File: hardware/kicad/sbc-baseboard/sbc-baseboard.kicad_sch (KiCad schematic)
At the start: 4 parts

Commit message: Re-lay out every sheet around its main component
Nets fan out of each hub IC as wires at pin pitch; connectors, series
parts, pull-ups and power symbols sit at the lane ends, and labels are
kept for nets that leave the page. Supply pins share a bus with their
decoupling; ESD arrays sit on the connector's D-/D+ rows and port
switches on the VBUS row, so every wire into a receptacle is straight;
the stacked USB-A is a two-unit symbol, one per port. Relays move to
their own sheet (8xx). ESD diodes use KiCad's PESD5V0S1UL in SOD-882.

Generator: gen/fanout.py (lane engine), gen/check_geom.py (endpoint
contacts), gen/netcheck.py (wire-level rail merges). ERC, both checks
and a renumbering-tolerant netlist diff against the first pass all
clean; 331 parts, 354 nets.

Co-Authored-By: Claude Fable 5.1 <noreply@anthropic.com>
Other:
- added sheet Relays (relays.kicad_sch)
- note added: "- K803 JW1FSN contact pad mapping (COM 6 / NO 4 / NC 2) against the Panasonic drawing"
- note added: "Reference designators: 1xx power, 2xx MCU, 3xx Ethernet, 4xx hub, 5xx FTDI, 6xx DAPLink, 7xx target I/O, 8xx relays and passthrough."
- note removed: "- K703 JW1FSN contact pad mapping (COM 6 / NO 4 / NC 2) against the Panasonic drawing"
- note removed: "Reference designators: 1xx power, 2xx MCU, 3xx Ethernet, 4xx hub, 5xx FTDI, 6xx DAPLink, 7xx target I/O."
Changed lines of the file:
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@@
 		(instances
 			(project "sbc-baseboard"
-				(path "/f7384331-47cf-4f51-a3a4-f7288a6fca1f"
+				(path "/67f2ab7f-7b0b-43bf-9ea7-cdb92436ed71"
 					(page "2")
 				)
@@
 		(instances
 			(project "sbc-baseboard"
-				(path "/f7384331-47cf-4f51-a3a4-f7288a6fca1f"
+				(path "/67f2ab7f-7b0b-43bf-9ea7-cdb92436ed71"
 					(page "3")
 				)
@@
 		(instances
 			(project "sbc-baseboard"
-				(path "/f7384331-47cf-4f51-a3a4-f7288a6fca1f"
+				(path "/67f2ab7f-7b0b-43bf-9ea7-cdb92436ed71"
 					(page "4")
 				)
@@
 		(instances
 			(project "sbc-baseboard"
-				(path "/f7384331-47cf-4f51-a3a4-f7288a6fca1f"
+				(path "/67f2ab7f-7b0b-43bf-9ea7-cdb92436ed71"
 					(page "5")
 				)
@@
 		(instances
 			(project "sbc-baseboard"
-				(path "/f7384331-47cf-4f51-a3a4-f7288a6fca1f"
+				(path "/67f2ab7f-7b0b-43bf-9ea7-cdb92436ed71"
 					(page "6")
 				)
@@
 		(instances
 			(project "sbc-baseboard"
-				(path "/f7384331-47cf-4f51-a3a4-f7288a6fca1f"
+				(path "/67f2ab7f-7b0b-43bf-9ea7-cdb92436ed71"
 					(page "7")
 				)
@@
 		(instances
 			(project "sbc-baseboard"
-				(path "/f7384331-47cf-4f51-a3a4-f7288a6fca1f"
+				(path "/67f2ab7f-7b0b-43bf-9ea7-cdb92436ed71"
 					(page "8")
+				)
+			)
+		)
+	)
+	(sheet
+		(at 210 80)
+		(size 50 25)
+		(exclude_from_sim no)
+		(in_bom yes)
+		(on_board yes)
+		(dnp no)
+		(fields_autoplaced yes)
+		(stroke
+			(width 0.1524)
+			(type solid)
+		)
+		(fill
+			(color 0 0 0 0)
+		)
+		(property "Sheetname" "Relays"
+			(at 210 79.2884 0)
+			(show_name no)
+			(do_not_autoplace no)
+			(effects
+				(font
+					(size 1.27 1.27)
+				)
+				(justify left bottom)
+			)
+		)
+		(property "Sheetfile" "relays.kicad_sch"
+			(at 210 105.5846 0)
+			(show_name no)
+			(do_not_autoplace no)
+			(effects
+				(font
+					(size 1.27 1.27)
+				)
+				(justify left top)
+			)
+		)
+		(instances
+			(project "sbc-baseboard"
+				(path "/67f2ab7f-7b0b-43bf-9ea7-cdb92436ed71"
+					(page "9")
 				)
 			)
@@
 		(instances
 			(project "sbc-baseboard"
-				(path "/f7384331-47cf-4f51-a3a4-f7288a6fca1f"
+				(path "/67f2ab7f-7b0b-43bf-9ea7-cdb92436ed71"
 					(reference "H1")
 					(unit 1)
@@
 		(instances
 			(project "sbc-baseboard"
-				(path "/f7384331-47cf-4f51-a3a4-f7288a6fca1f"
+				(path "/67f2ab7f-7b0b-43bf-9ea7-cdb92436ed71"
 					(reference "#PWR01001")
 					(unit 1)
@@
 		(instances
 			(project "sbc-baseboard"
-				(path "/f7384331-47cf-4f51-a3a4-f7288a6fca1f"
+				(path "/67f2ab7f-7b0b-43bf-9ea7-cdb92436ed71"
 					(reference "H2")
 					(unit 1)
@@
 		(instances
 			(project "sbc-baseboard"
-				(path "/f7384331-47cf-4f51-a3a4-f7288a6fca1f"
+				(path "/67f2ab7f-7b0b-43bf-9ea7-cdb92436ed71"
 					(reference "#PWR01002")
 					(unit 1)
@@
 		(instances
 			(project "sbc-baseboard"
-				(path "/f7384331-47cf-4f51-a3a4-f7288a6fca1f"
+				(path "/67f2ab7f-7b0b-43bf-9ea7-cdb92436ed71"
 					(reference "H3")
 					(unit 1)
@@
 		(instances
 			(project "sbc-baseboard"
-				(path "/f7384331-47cf-4f51-a3a4-f7288a6fca1f"
+				(path "/67f2ab7f-7b0b-43bf-9ea7-cdb92436ed71"
 					(reference "#PWR01003")
 					(unit 1)
@@
 		(instances
 			(project "sbc-baseboard"
-				(path "/f7384331-47cf-4f51-a3a4-f7288a6fca1f"
+				(path "/67f2ab7f-7b0b-43bf-9ea7-cdb92436ed71"
 					(reference "H4")
 					(unit 1)
@@
 		(instances
 			(project "sbc-baseboard"
-				(path "/f7384331-47cf-4f51-a3a4-f7288a6fca1f"
+				(path "/67f2ab7f-7b0b-43bf-9ea7-cdb92436ed71"
 					(reference "#PWR01004")
 					(unit 1)
@@
 		)
 	)
-	(text "  - K703 JW1FSN contact pad mapping (COM 6 / NO 4 / NC 2) against the Panasonic drawing"
+	(text "  - K803 JW1FSN contact pad mapping (COM 6 / NO 4 / NC 2) against the Panasonic drawing"
 		(exclude_from_sim no)
 		(at 30 194.2 0)
@@
 		)
 	)
-	(text "Reference designators: 1xx power, 2xx MCU, 3xx Ethernet, 4xx hub, 5xx FTDI, 6xx DAPLink, 7xx target I/O."
+	(text "Reference designators: 1xx power, 2xx MCU, 3xx Ethernet, 4xx hub, 5xx FTDI, 6xx DAPLink, 7xx target I/O, 8xx relays and passthrough."
 		(exclude_from_sim no)
 		(at 30 213.4 0)

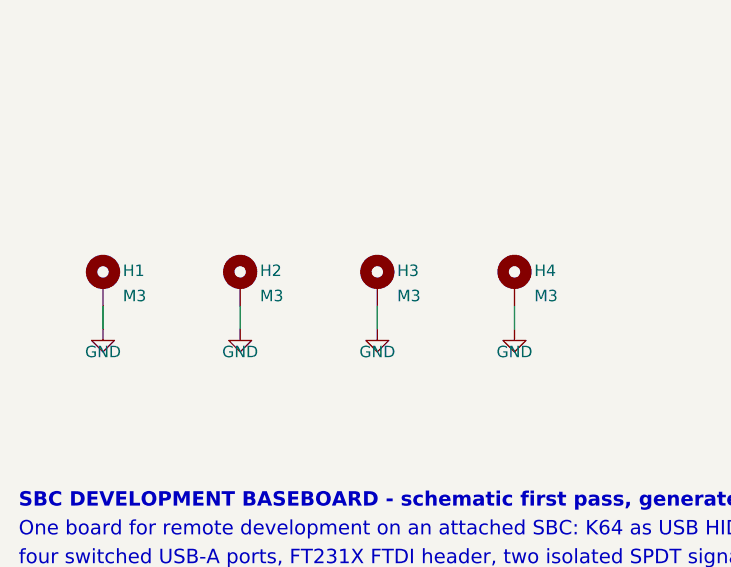
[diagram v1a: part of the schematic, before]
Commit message: Symbol direction, field text and decoupling ladders across every sheet
Every GND symbol now hangs down and every rail stands up: decoupling
hangs from the supply bus into a GND rail with one GND symbol at the end
(ladders), rails on crowded supply pins are jogged sideways, the SWD
header is mirrored instead of rotated. Field text on in-line parts reads
horizontally (KiCad adds the symbol rotation to the field angle) and is
placed by lane direction; hanging parts carry their text on the side away
from the pin; IC reference and value sit where the library put them.
Power sheet: bus buffer moved under the STUSB4500's I2C lanes with direct
routes, programmer by label, buck drawn as a box with its input and
output capacitors as ladders. New gen/check_layout.py reports text and
wire overlaps and wrong-way power symbols; PDF export draws hop-overs.

ERC 0, no merged rails, netlist equivalent; text-overlap residue listed
in the layout checker output remains on the hub, relays and DAPLink.

Co-Authored-By: Claude Fable 5.1 <noreply@anthropic.com>
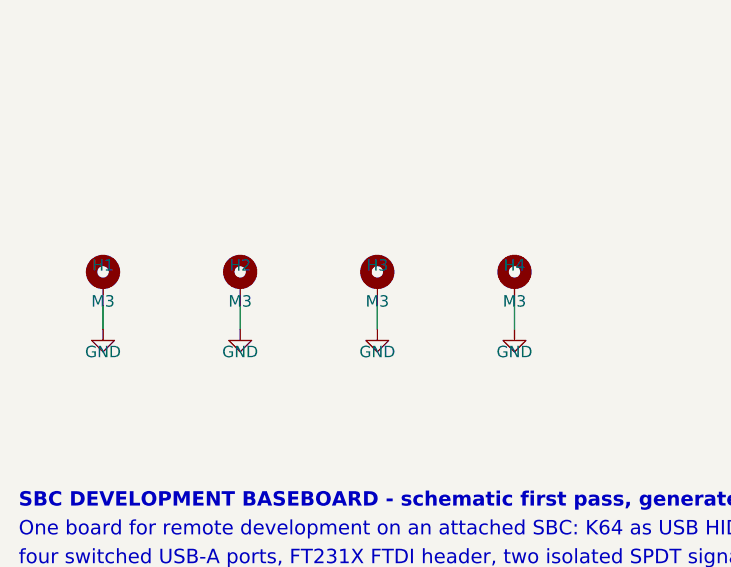
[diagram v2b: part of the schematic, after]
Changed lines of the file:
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@@
 		(instances
 			(project "sbc-baseboard"
-				(path "/67f2ab7f-7b0b-43bf-9ea7-cdb92436ed71"
+				(path "/720ca2c9-6349-4d12-b50d-43ef6cb86535"
 					(page "2")
 				)
@@
 		(instances
 			(project "sbc-baseboard"
-				(path "/67f2ab7f-7b0b-43bf-9ea7-cdb92436ed71"
+				(path "/720ca2c9-6349-4d12-b50d-43ef6cb86535"
 					(page "3")
 				)
@@
 		(instances
 			(project "sbc-baseboard"
-				(path "/67f2ab7f-7b0b-43bf-9ea7-cdb92436ed71"
+				(path "/720ca2c9-6349-4d12-b50d-43ef6cb86535"
 					(page "4")
 				)
@@
 		(instances
 			(project "sbc-baseboard"
-				(path "/67f2ab7f-7b0b-43bf-9ea7-cdb92436ed71"
+				(path "/720ca2c9-6349-4d12-b50d-43ef6cb86535"
 					(page "5")
 				)
@@
 		(instances
 			(project "sbc-baseboard"
-				(path "/67f2ab7f-7b0b-43bf-9ea7-cdb92436ed71"
+				(path "/720ca2c9-6349-4d12-b50d-43ef6cb86535"
 					(page "6")
 				)
@@
 		(instances
 			(project "sbc-baseboard"
-				(path "/67f2ab7f-7b0b-43bf-9ea7-cdb92436ed71"
+				(path "/720ca2c9-6349-4d12-b50d-43ef6cb86535"
 					(page "7")
 				)
@@
 		(instances
 			(project "sbc-baseboard"
-				(path "/67f2ab7f-7b0b-43bf-9ea7-cdb92436ed71"
+				(path "/720ca2c9-6349-4d12-b50d-43ef6cb86535"
 					(page "8")
 				)
@@
 		(instances
 			(project "sbc-baseboard"
-				(path "/67f2ab7f-7b0b-43bf-9ea7-cdb92436ed71"
+				(path "/720ca2c9-6349-4d12-b50d-43ef6cb86535"
 					(page "9")
 				)
@@
 		(fields_autoplaced no)
 		(property "Reference" "H1"
-			(at 41.57 148.46 0)
-			(show_name no)
-			(do_not_autoplace no)
-			(effects
-				(font
-					(size 1.27 1.27)
-				)
-				(justify left)
+			(at 39.37 147.86 0)
+			(show_name no)
+			(do_not_autoplace no)
+			(effects
+				(font
+					(size 1.27 1.27)
+				)
 			)
 		)
 		(property "Value" "M3"
-			(at 41.57 151.26 0)
-			(show_name no)
-			(do_not_autoplace no)
-			(effects
-				(font
-					(size 1.27 1.27)
-				)
-				(justify left)
+			(at 39.37 151.86 0)
+			(show_name no)
+			(do_not_autoplace no)
+			(effects
+				(font
+					(size 1.27 1.27)
+				)
 			)
 		)
@@
 					(size 1.27 1.27)
 				)
-				(justify left)
 			)
 		)
@@
 					(size 1.27 1.27)
 				)
-				(justify left)
 			)
 		)
@@
 					(size 1.27 1.27)
 				)
-				(justify left)
 			)
 		)
@@
 		(instances
 			(project "sbc-baseboard"
-				(path "/67f2ab7f-7b0b-43bf-9ea7-cdb92436ed71"
+				(path "/720ca2c9-6349-4d12-b50d-43ef6cb86535"
 					(reference "H1")
 					(unit 1)
@@
 		(instances
 			(project "sbc-baseboard"
-				(path "/67f2ab7f-7b0b-43bf-9ea7-cdb92436ed71"
+				(path "/720ca2c9-6349-4d12-b50d-43ef6cb86535"
 					(reference "#PWR01001")
 					(unit 1)
@@
 		(fields_autoplaced no)
 		(property "Reference" "H2"
-			(at 56.81 148.46 0)
-			(show_name no)
-			(do_not_autoplace no)
-			(effects
-				(font
-					(size 1.27 1.27)
-				)
-				(justify left)
+			(at 54.61 147.86 0)
+			(show_name no)
+			(do_not_autoplace no)
+			(effects
+				(font
+					(size 1.27 1.27)
+				)
 			)
 		)
 		(property "Value" "M3"
-			(at 56.81 151.26 0)
-			(show_name no)
-			(do_not_autoplace no)
-			(effects
-				(font
-					(size 1.27 1.27)
-				)
-				(justify left)
+			(at 54.61 151.86 0)
+			(show_name no)
+			(do_not_autoplace no)
+			(effects
+				(font
+					(size 1.27 1.27)
+				)
 			)
 		)
@@
 					(size 1.27 1.27)
 				)
-				(justify left)
 			)
 		)
@@
 					(size 1.27 1.27)
 				)
-				(justify left)
 			)
 		)
@@
 					(size 1.27 1.27)
 				)
-				(justify left)
 			)
 		)
@@
 		(instances
 			(project "sbc-baseboard"
-				(path "/67f2ab7f-7b0b-43bf-9ea7-cdb92436ed71"
+				(path "/720ca2c9-6349-4d12-b50d-43ef6cb86535"
 					(reference "H2")
 					(unit 1)
@@
 		(instances
 			(project "sbc-baseboard"
-				(path "/67f2ab7f-7b0b-43bf-9ea7-cdb92436ed71"
+				(path "/720ca2c9-6349-4d12-b50d-43ef6cb86535"
 					(reference "#PWR01002")
 					(unit 1)
@@
 		(fields_autoplaced no)
 		(property "Reference" "H3"
-			(at 72.05 148.46 0)
-			(show_name no)
-			(do_not_autoplace no)
-			(effects
-				(font
-					(size 1.27 1.27)
-				)
-				(justify left)
+			(at 69.85 147.86 0)
+			(show_name no)
+			(do_not_autoplace no)
+			(effects
+				(font
+					(size 1.27 1.27)
+				)
 			)
 		)
 		(property "Value" "M3"
-			(at 72.05 151.26 0)
-			(show_name no)
-			(do_not_autoplace no)
-			(effects
-				(font
-					(size 1.27 1.27)
-				)
-				(justify left)
+			(at 69.85 151.86 0)
+			(show_name no)
+			(do_not_autoplace no)
+			(effects
+				(font
+					(size 1.27 1.27)
+				)
 			)
 		)
@@
 					(size 1.27 1.27)
 				)
-				(justify left)
 			)
 		)
@@
 					(size 1.27 1.27)
 				)
-				(justify left)
 			)
 		)
@@
 					(size 1.27 1.27)
 				)
-				(justify left)
 			)
 		)
@@
 		(instances
 			(project "sbc-baseboard"
-				(path "/67f2ab7f-7b0b-43bf-9ea7-cdb92436ed71"
+				(path "/720ca2c9-6349-4d12-b50d-43ef6cb86535"
 					(reference "H3")
 					(unit 1)
@@
 		(instances
 			(project "sbc-baseboard"
-				(path "/67f2ab7f-7b0b-43bf-9ea7-cdb92436ed71"
+				(path "/720ca2c9-6349-4d12-b50d-43ef6cb86535"
 					(reference "#PWR01003")
 					(unit 1)
@@
 		(fields_autoplaced no)
 		(property "Reference" "H4"
-			(at 87.29 148.46 0)
-			(show_name no)
-			(do_not_autoplace no)
-			(effects
-				(font
-					(size 1.27 1.27)
-				)
-				(justify left)
+			(at 85.09 147.86 0)
+			(show_name no)
+			(do_not_autoplace no)
+			(effects
+				(font
+					(size 1.27 1.27)
+				)
 			)
 		)
 		(property "Value" "M3"
-			(at 87.29 151.26 0)
-			(show_name no)
-			(do_not_autoplace no)
-			(effects
-				(font
-					(size 1.27 1.27)
-				)
-				(justify left)
+			(at 85.09 151.86 0)
+			(show_name no)
+			(do_not_autoplace no)
+			(effects
+				(font
+					(size 1.27 1.27)
+				)
 			)
 		)
@@
 					(size 1.27 1.27)
 				)
-				(justify left)
 			)
 		)
@@
 					(size 1.27 1.27)
 				)
-				(justify left)
 			)
 		)
@@
 					(size 1.27 1.27)
 				)
-				(justify left)
 			)
 		)
@@
 		(instances
 			(project "sbc-baseboard"
-				(path "/67f2ab7f-7b0b-43bf-9ea7-cdb92436ed71"
+				(path "/720ca2c9-6349-4d12-b50d-43ef6cb86535"
 					(reference "H4")
 					(unit 1)
@@
 		(instances
 			(project "sbc-baseboard"
-				(path "/67f2ab7f-7b0b-43bf-9ea7-cdb92436ed71"
+				(path "/720ca2c9-6349-4d12-b50d-43ef6cb86535"
 					(reference "#PWR01004")
 					(unit 1)
